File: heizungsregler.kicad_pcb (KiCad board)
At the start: 2 copper layers, 3 parts, among them J101 RPi_GPIO, J105 Conn_01x04_Male, U101 oled_0.96

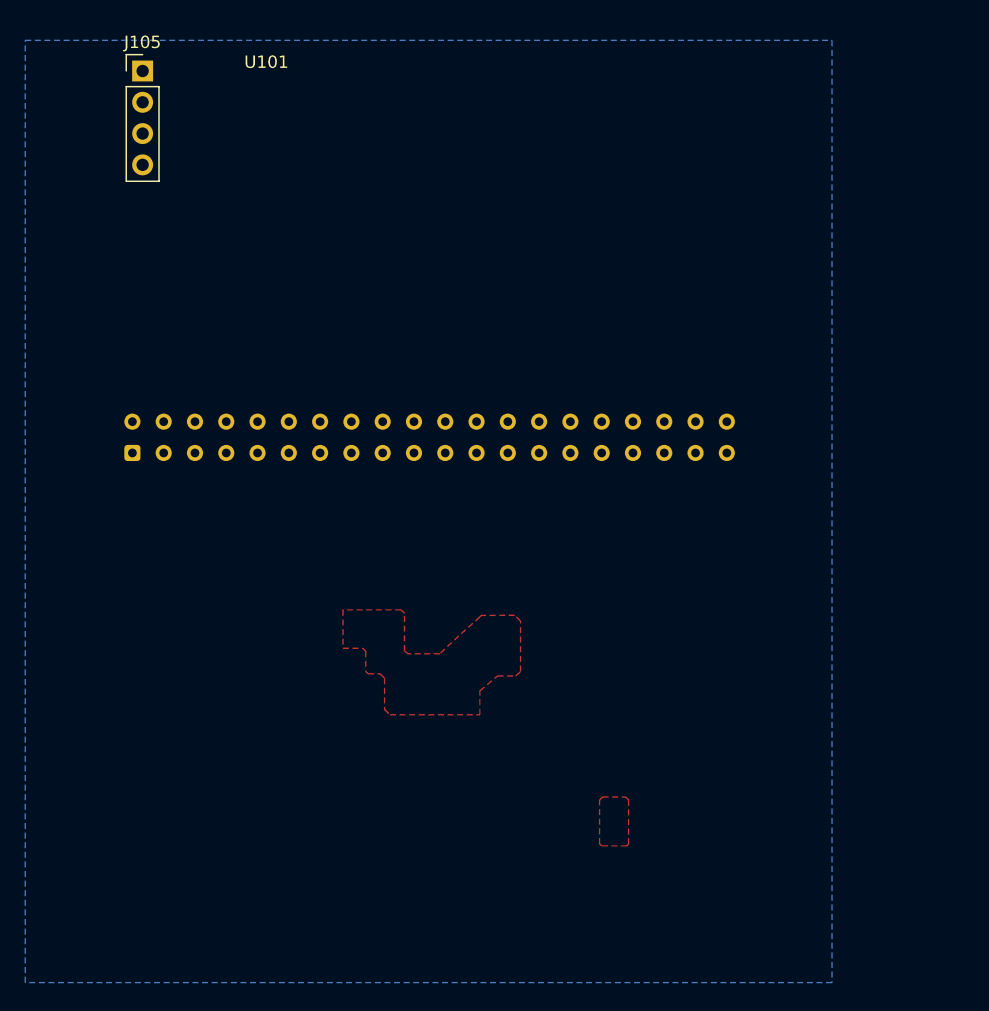
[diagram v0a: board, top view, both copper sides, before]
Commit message: Masseflächen zwischen Leitungen
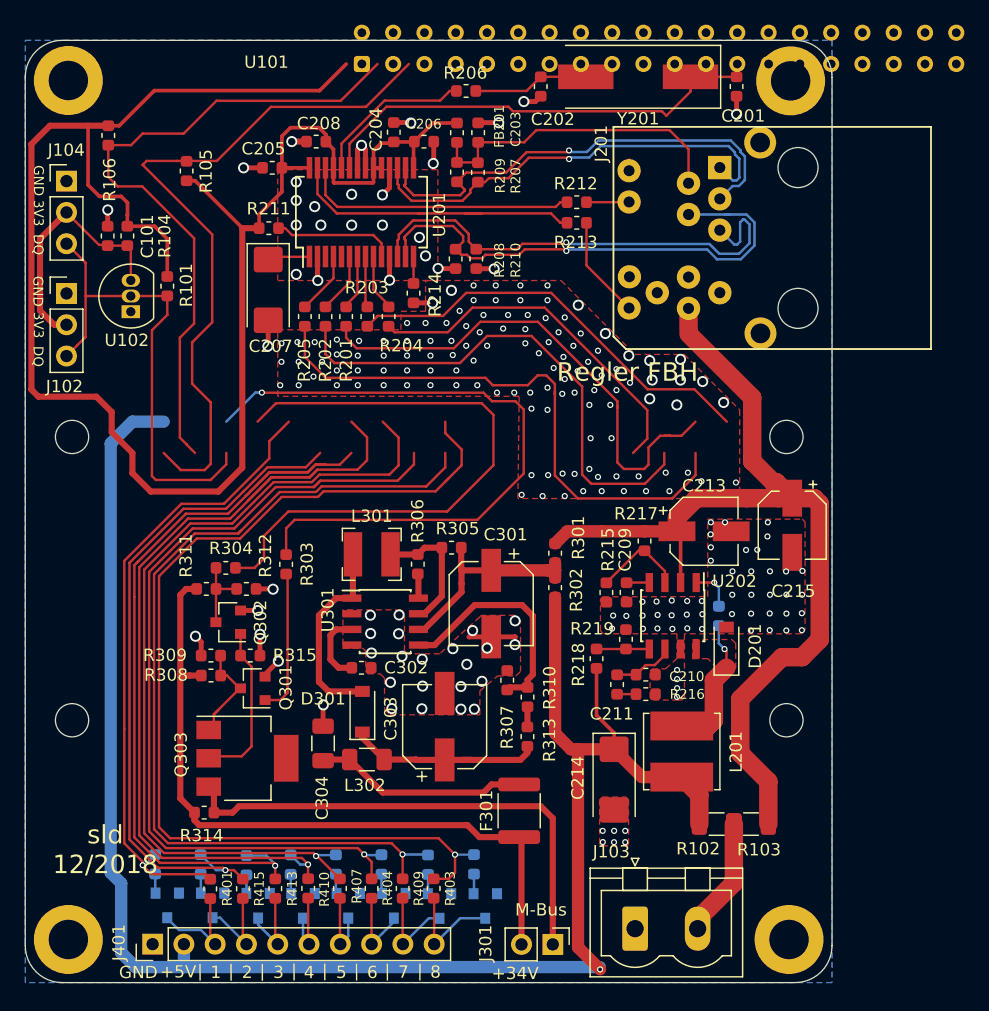
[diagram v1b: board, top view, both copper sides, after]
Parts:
- removed J101: RPi_GPIO, Connector_Samtec_HLE_THT:Samtec_HLE-120-02-xx-DV-TE_2x20_P2.54mm_Horizontal
- removed J105: Conn_01x04_Male, Connector_PinHeader_2.54mm:PinHeader_1x04_P2.54mm_Vertical
- added C101: C, Capacitor_SMD:C_0603_1608Metric, F.Cu at (120.2, 67.4)
- added C201: 22P, Capacitor_SMD:C_0603_1608Metric, F.Cu at (171.2, 55.2)
- added C202: 22P, Capacitor_SMD:C_0603_1608Metric, F.Cu at (155.3, 55.2)
- added C203: 100N, Capacitor_SMD:C_0603_1608Metric, F.Cu at (150.3, 59.0)
- added C204: 100N, Capacitor_SMD:C_0603_1608Metric, F.Cu at (143.4, 59.0)
- added C205: 100N, Capacitor_SMD:C_0603_1608Metric, F.Cu at (133.6, 61.9)
- added C206: 100N, Capacitor_SMD:C_0603_1608Metric, F.Cu at (145.9, 59.7)
- added C207: 10U, Capacitor_Tantalum_SMD:CP_EIA-6032-28_Kemet-C, F.Cu at (133.2, 71.8)
- added C208: 100N, Capacitor_SMD:C_0603_1608Metric, F.Cu at (137.1, 59.7)
- added C209: 8N2, Capacitor_SMD:C_0603_1608Metric, F.Cu at (162.3, 96.3)
- added C210: 82P, Capacitor_SMD:C_0603_1608Metric, F.Cu at (163.9, 103.0)
- added C211: 4N3, Capacitor_SMD:C_0603_1608Metric, F.Cu at (161.6, 103.8)
- added C212: 100N, Capacitor_SMD:C_0603_1608Metric, B.Cu at (169.8, 98.2)
- added C213: 10U, Capacitor_SMD:CP_Elec_5x5.4, F.Cu at (168.6, 91.4)
- added C214: 47U, Capacitor_Tantalum_SMD:CP_EIA-6032-28_Kemet-C, F.Cu at (161.3, 111.5)
- added C215: 10U, Capacitor_SMD:CP_Elec_5x5.4, F.Cu at (175.8, 90.9)
- added C301: 22U, Capacitor_SMD:CP_Elec_6.3x5.7, F.Cu at (151.3, 97.2)
- added C302: 330P, Capacitor_SMD:C_0603_1608Metric, F.Cu at (140.8, 102.4)
- added C303: 47U, Capacitor_SMD:CP_Elec_6.3x7.7, F.Cu at (147.6, 107.2)
- added C304: 1U, Capacitor_SMD:C_1206_3216Metric, F.Cu at (137.7, 108.6)
- added D201: D_Schottky, Diode_SMD:D_SOD-123, F.Cu at (170.4, 100.8)
- added D301: D_Schottky, Diode_SMD:D_SOD-123, F.Cu at (140.9, 106.0)
- added F301: Fuse 2A, Fuse:Fuse_1812_4532Metric, F.Cu at (153.6, 114.0)
- added FB201: Ferrite_Bead, Inductor_SMD:L_0603_1608Metric, F.Cu at (148.6, 59.0)
- added H101: MountingHole, MountingHole:MountingHole_2.7mm_M2.5_DIN965, F.Cu at (117.3, 106.7)
- added H102: MountingHole, MountingHole:MountingHole_2.7mm_M2.5_DIN965, F.Cu at (175.3, 106.7)
- added H103: MountingHole, MountingHole:MountingHole_2.7mm_M2.5_DIN965, F.Cu at (175.3, 83.7)
- added H104: MountingHole, MountingHole:MountingHole_2.7mm_M2.5_DIN965, F.Cu at (117.3, 83.7)
- added H105: MountingHole, MountingHole:MountingHole_3.2mm_M3_DIN965_Pad, F.Cu at (175.6, 54.8)
- added H106: MountingHole, MountingHole:MountingHole_3.2mm_M3_DIN965_Pad, F.Cu at (117.0, 124.5)
- added H107: MountingHole, MountingHole:MountingHole_3.2mm_M3_DIN965_Pad, F.Cu at (175.5, 124.5)
- added H108: MountingHole, MountingHole:MountingHole_3.2mm_M3_DIN965_Pad, F.Cu at (117.0, 54.8)
- added J102: Conn_01x03_Male, Connector_PinHeader_2.54mm:PinHeader_1x03_P2.54mm_Vertical, F.Cu at (116.8, 72.0)
- added J103: Conn_01x02, Connector_Phoenix_MSTB:PhoenixContact_MSTBVA_2,5_2-G-5,08_1x02_P5.08mm_Vertical, F.Cu at (163.0, 123.6)
- added J104: Conn_01x03_Male, Connector_PinHeader_2.54mm:PinHeader_1x03_P2.54mm_Vertical, F.Cu at (116.8, 62.9)
- added J201: SI-52008-F, kicadlibs:RJ45_BEL_STEWART_SI-52008-F, F.Cu at (169.9, 61.8)
- added J301: Conn_01x02_Male, Connector_PinHeader_2.54mm:PinHeader_1x02_P2.54mm_Vertical, F.Cu at (156.3, 124.9)
- added J401: Conn_01x10_Male, Connector_PinHeader_2.54mm:PinHeader_1x10_P2.54mm_Vertical, F.Cu at (123.8, 124.9)
- added L201: 22U, Inductor_SMD:L_Bourns_SRN6045TA, F.Cu at (166.8, 109.2)
- added L301: 150U, Inductor_SMD:L_Bourns-SRN4018, F.Cu at (141.6, 93.2)
- added L302: 1U, Inductor_SMD:L_1206_3216Metric, F.Cu at (141.2, 109.9)
- added Q301: BC847, Package_TO_SOT_SMD:SOT-23, F.Cu at (132.0, 104.1)
- added Q302: BC847, Package_TO_SOT_SMD:SOT-23, F.Cu at (130.0, 98.7)
- added Q303: BCP51, Package_TO_SOT_SMD:SOT-223, F.Cu at (131.5, 109.8)
- added Q401: BC847, Package_TO_SOT_SMD:SOT-23, B.Cu at (125.0, 121.7)
- added Q402: BC847, Package_TO_SOT_SMD:SOT-23, B.Cu at (150.8, 121.8)
- added Q403: BC847, Package_TO_SOT_SMD:SOT-23, B.Cu at (143.4, 121.8)
- added Q404: BC847, Package_TO_SOT_SMD:SOT-23, B.Cu at (139.7, 121.8)
- added Q405: BC847, Package_TO_SOT_SMD:SOT-23, B.Cu at (147.1, 121.8)
- added Q406: BC847, Package_TO_SOT_SMD:SOT-23, B.Cu at (136.1, 121.8)
- added Q407: BC847, Package_TO_SOT_SMD:SOT-23, B.Cu at (132.4, 121.8)
- added Q408: BC847, Package_TO_SOT_SMD:SOT-23, B.Cu at (128.7, 121.7)
- added R101: R, Resistor_SMD:R_0603_1608Metric, F.Cu at (125.0, 71.5)
- added R102: 0R00, Resistor_SMD:R_1206_3216Metric, F.Cu at (169.6, 115.1)
- added R103: 0R00, Resistor_SMD:R_1206_3216Metric, F.Cu at (172.4, 115.1)
- added R104: R, Resistor_SMD:R_0603_1608Metric, F.Cu at (121.8, 67.4)
- added R105: 2K2, Resistor_SMD:R_0603_1608Metric, F.Cu at (126.6, 62.1)
- added R106: 2K2, Resistor_SMD:R_0603_1608Metric, F.Cu at (120.2, 59.2)
- added R201: 0R00, Resistor_SMD:R_0603_1608Metric, F.Cu at (139.6, 73.9)
- added R202: 0R00, Resistor_SMD:R_0603_1608Metric, F.Cu at (137.9, 73.9)
- added R203: 0R00, Resistor_SMD:R_0603_1608Metric, F.Cu at (141.3, 73.9)
- added R204: 0R00, Resistor_SMD:R_0603_1608Metric, F.Cu at (143.0, 73.9)
- added R205: 0R00, Resistor_SMD:R_0603_1608Metric, F.Cu at (136.2, 73.9)
- added R206: 0R00, Resistor_SMD:R_0603_1608Metric, F.Cu at (149.3, 55.6)
- added R207: 49R9, Resistor_SMD:R_0603_1608Metric, F.Cu at (150.2, 62.2)
- added R208: 49R9, Resistor_SMD:R_0603_1608Metric, F.Cu at (148.4, 69.2)
- added R209: 49R9, Resistor_SMD:R_0603_1608Metric, F.Cu at (148.6, 62.2)
- added R210: 49R9, Resistor_SMD:R_0603_1608Metric, F.Cu at (150.1, 69.2)
- added R211: 0R00, Resistor_SMD:R_0603_1608Metric, F.Cu at (133.3, 66.8)
- added R212: 220R, Resistor_SMD:R_0603_1608Metric, F.Cu at (158.3, 64.6)
- added R213: 220R, Resistor_SMD:R_0603_1608Metric, F.Cu at (158.3, 66.3)
- added R214: 2K32, Resistor_SMD:R_0603_1608Metric, F.Cu at (145.0, 72.0)
- added R215: 19K6, Resistor_SMD:R_0603_1608Metric, F.Cu at (160.7, 96.3)
- added R216: 18K7, Resistor_SMD:R_0603_1608Metric, F.Cu at (163.9, 104.6)
- added R217: 169K, Resistor_SMD:R_0603_1608Metric, F.Cu at (163.8, 92.2)
- added R218: 10K2, Resistor_SMD:R_0603_1608Metric, F.Cu at (159.9, 101.7)
- added R219: 1K96, Resistor_SMD:R_0603_1608Metric, F.Cu at (162.3, 100.1)
- added R301: 0R00, Resistor_SMD:R_0603_1608Metric, F.Cu at (156.5, 93.1)
- added R302: 0R00, Resistor_SMD:R_0603_1608Metric, F.Cu at (156.5, 95.9)
- added R303: 1K, Resistor_SMD:R_0603_1608Metric, F.Cu at (134.7, 94.0)
- added R304: 1K, Resistor_SMD:R_0603_1608Metric, F.Cu at (129.8, 94.3)
- added R305: 0R47, Resistor_SMD:R_0603_1608Metric, F.Cu at (148.1, 92.7)
- added R306: 180, Resistor_SMD:R_0603_1608Metric, F.Cu at (145.4, 94.0)
- added R307: 4k7, Resistor_SMD:R_0603_1608Metric, F.Cu at (152.6, 103.5)
- added R308: 39K, Resistor_SMD:R_0603_1608Metric, F.Cu at (128.6, 103.1)
- added R309: 22K, Resistor_SMD:R_0603_1608Metric, F.Cu at (128.6, 101.5)
- added R310: 100K, Resistor_SMD:R_0603_1608Metric, F.Cu at (154.3, 104.8)
- added R311: 33K, Resistor_SMD:R_0603_1608Metric, F.Cu at (128.2, 96.0)
- added R312: 3K3, Resistor_SMD:R_0603_1608Metric, F.Cu at (131.5, 96.0)
- added R313: 22K, Resistor_SMD:R_0603_1608Metric, F.Cu at (154.3, 108.0)
- added R314: 220K, Resistor_SMD:R_0603_1608Metric, F.Cu at (128.0, 114.2)
- added R315: 82R, Resistor_SMD:R_0603_1608Metric, F.Cu at (131.8, 101.5)
- added R401: R, Resistor_SMD:R_0603_1608Metric, F.Cu at (128.5, 120.4)
- added R402: R, Resistor_SMD:R_0603_1608Metric, B.Cu at (124.0, 118.4)
- added R403: R, Resistor_SMD:R_0603_1608Metric, F.Cu at (146.7, 120.4)
- added R404: R, Resistor_SMD:R_0603_1608Metric, F.Cu at (141.6, 120.4)
- added R405: R, Resistor_SMD:R_0603_1608Metric, B.Cu at (149.9, 118.4)
- added R406: R, Resistor_SMD:R_0603_1608Metric, B.Cu at (142.4, 118.4)
- added R407: R, Resistor_SMD:R_0603_1608Metric, F.Cu at (139.1, 120.4)
- added R408: R, Resistor_SMD:R_0603_1608Metric, B.Cu at (138.7, 118.4)
- added R409: R, Resistor_SMD:R_0603_1608Metric, F.Cu at (144.1, 120.4)
- added R410: R, Resistor_SMD:R_0603_1608Metric, F.Cu at (136.5, 120.3)
- added R411: R, Resistor_SMD:R_0603_1608Metric, B.Cu at (146.2, 118.4)
- added R412: R, Resistor_SMD:R_0603_1608Metric, B.Cu at (135.1, 118.4)
- added R413: R, Resistor_SMD:R_0603_1608Metric, F.Cu at (133.8, 120.4)
- added R414: R, Resistor_SMD:R_0603_1608Metric, B.Cu at (131.5, 118.5)
- added R415: R, Resistor_SMD:R_0603_1608Metric, F.Cu at (131.2, 120.4)
- added R416: R, Resistor_SMD:R_0603_1608Metric, B.Cu at (127.7, 118.4)
- added U102: DS18B20, Package_TO_SOT_THT:TO-92_Inline, F.Cu at (122.1, 73.5)
- added U201: ENC28J60x-SS, Package_SO:SSOP-28_5.3x10.2mm_P0.65mm, F.Cu at (140.8, 65.5)
- added U202: TPS54231, Package_SO:SOIC-8_3.9x4.9mm_P1.27mm, F.Cu at (166.1, 98.2)
- added U301: MC34063AD, Package_SO:SOIC-8_3.9x4.9mm_P1.27mm, F.Cu at (142.7, 98.7)
- added Y201: Crystal, Crystal:Crystal_SMD_HC49-SD, F.Cu at (163.3, 54.5)
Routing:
- net +3V3: track 0.00 -> 152.0 mm
- net +5V: track 0.00 -> 141.0 mm, vias 0 -> 1
- net /REL8: track 0.00 -> 83.1 mm, vias 0 -> 1
- net +24V: track 0.00 -> 77.8 mm
- net /REL7: track 0.00 -> 74.6 mm, vias 0 -> 1
- net /REL4: track 0.00 -> 71.8 mm, vias 0 -> 1
- net /REL6: track 0.00 -> 69.6 mm, vias 0 -> 1
- net /REL5: track 0.00 -> 68.8 mm, vias 0 -> 1
- net /REL3: track 0.00 -> 67.4 mm, vias 0 -> 1
- net +36V: track 0.00 -> 57.7 mm
- net /SDA: track 0.00 -> 57.5 mm
- net /REL2: track 0.00 -> 54.7 mm, vias 0 -> 1
- net /SCL: track 0.00 -> 54.6 mm
- net /TXD: track 0.00 -> 54.2 mm, vias 0 -> 1
- net /REL1: track 0.00 -> 51.6 mm, vias 0 -> 1
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- added copper zone on F.Cu, net Net-(C212-Pad1)
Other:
- board outline added: 65.5 x 76.5 mm
- board text added: "+34V"
- board text added: "+5V"
- board text added: "1"
- board text added: "2"
- board text added: "3"
- board text added: "3V3"
- board text added: "4"
- board text added: "5"
- board text added: "6"
- board text added: "7"
- board text added: "8"
- board text added: "DQ"
- board text added: "GND"
- board text added: "M-Bus"
- board text added: "Regler FBH"
- board text added: "sld 12/2018"
- board text added: "|"

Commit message: Änderungen nach Review, Layout fertig
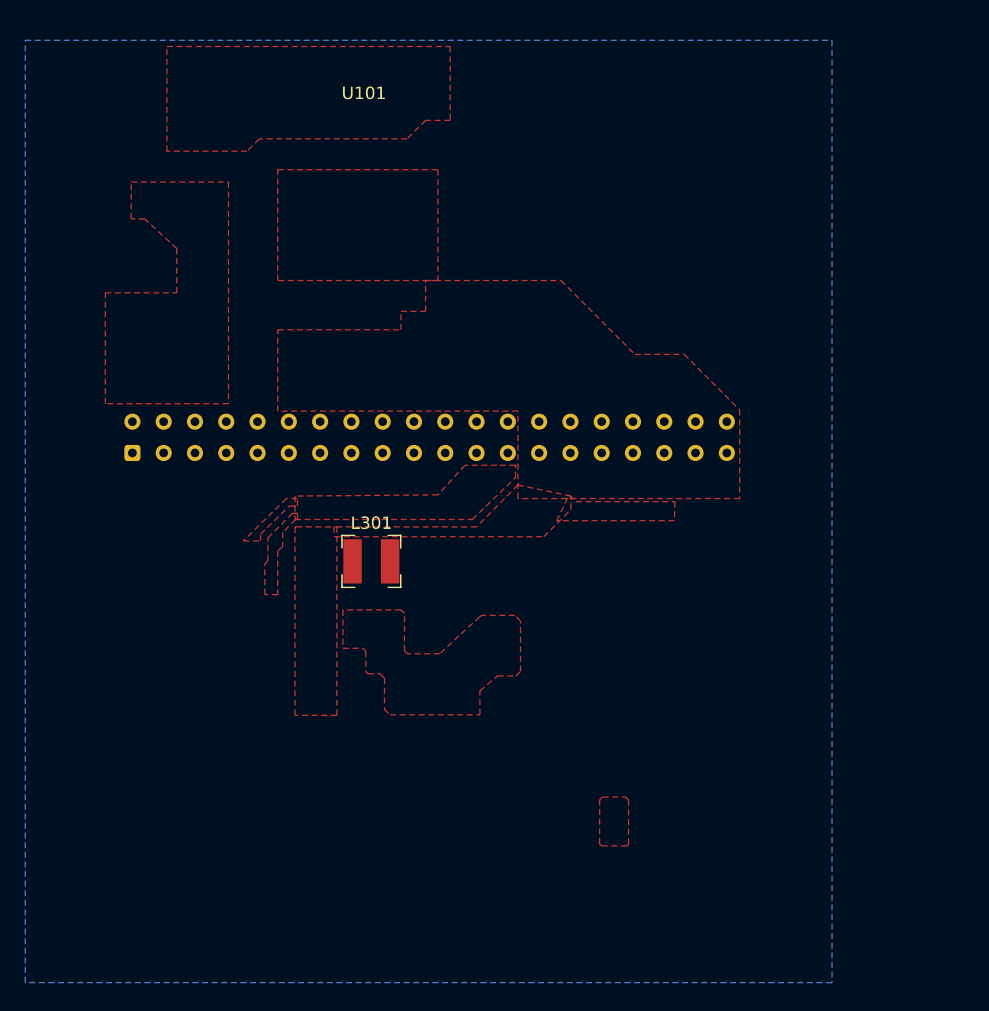
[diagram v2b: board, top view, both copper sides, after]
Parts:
- removed C101: C, Capacitor_SMD:C_0603_1608Metric
- removed C201, C202: 22P, Capacitor_SMD:C_0603_1608Metric
- removed C203, C204, C205, C206, C208, C212: 100N, Capacitor_SMD:C_0603_1608Metric
- removed C207: 10U, Capacitor_Tantalum_SMD:CP_EIA-6032-28_Kemet-C
- removed C209: 8N2, Capacitor_SMD:C_0603_1608Metric
- removed C210: 82P, Capacitor_SMD:C_0603_1608Metric
- removed C211: 4N3, Capacitor_SMD:C_0603_1608Metric
- removed C213, C215: 10U, Capacitor_SMD:CP_Elec_5x5.4
- removed C214: 47U, Capacitor_Tantalum_SMD:CP_EIA-6032-28_Kemet-C
- removed C301: 22U, Capacitor_SMD:CP_Elec_6.3x5.7
- removed C302: 330P, Capacitor_SMD:C_0603_1608Metric
- removed C303: 47U, Capacitor_SMD:CP_Elec_6.3x7.7
- removed C304: 1U, Capacitor_SMD:C_1206_3216Metric
- removed D201, D301: D_Schottky, Diode_SMD:D_SOD-123
- removed F301: Fuse 2A, Fuse:Fuse_1812_4532Metric
- removed FB201: Ferrite_Bead, Inductor_SMD:L_0603_1608Metric
- removed H101, H102, H103, H104: MountingHole, MountingHole:MountingHole_2.7mm_M2.5_DIN965
- removed H105, H106, H107, H108: MountingHole, MountingHole:MountingHole_3.2mm_M3_DIN965_Pad
- removed J102, J104: Conn_01x03_Male, Connector_PinHeader_2.54mm:PinHeader_1x03_P2.54mm_Vertical
- removed J103: Conn_01x02, Connector_Phoenix_MSTB:PhoenixContact_MSTBVA_2,5_2-G-5,08_1x02_P5.08mm_Vertical
- removed J201: SI-52008-F, kicadlibs:RJ45_BEL_STEWART_SI-52008-F
- removed J301: Conn_01x02_Male, Connector_PinHeader_2.54mm:PinHeader_1x02_P2.54mm_Vertical
- removed J401: Conn_01x10_Male, Connector_PinHeader_2.54mm:PinHeader_1x10_P2.54mm_Vertical
- removed L201: 22U, Inductor_SMD:L_Bourns_SRN6045TA
- removed L302: 1U, Inductor_SMD:L_1206_3216Metric
- removed Q301, Q302, Q401, Q402, Q403, Q404, Q405, Q406, Q407, Q408: BC847, Package_TO_SOT_SMD:SOT-23
- removed Q303: BCP51, Package_TO_SOT_SMD:SOT-223
- removed R101, R104, R401, R402, R403, R404, R405, R406, R407, R408, R409, R410, R411, R412, R413, R414, R415, R416: R, Resistor_SMD:R_0603_1608Metric
- removed R102, R103: 0R00, Resistor_SMD:R_1206_3216Metric
- removed R105, R106: 2K2, Resistor_SMD:R_0603_1608Metric
- removed R201, R202, R203, R204, R205, R206, R211, R301, R302: 0R00, Resistor_SMD:R_0603_1608Metric
- removed R207, R208, R209, R210: 49R9, Resistor_SMD:R_0603_1608Metric
- removed R212, R213: 220R, Resistor_SMD:R_0603_1608Metric
- removed R214: 2K32, Resistor_SMD:R_0603_1608Metric
- removed R215: 19K6, Resistor_SMD:R_0603_1608Metric
- removed R216: 18K7, Resistor_SMD:R_0603_1608Metric
- removed R217: 169K, Resistor_SMD:R_0603_1608Metric
- removed R218: 10K2, Resistor_SMD:R_0603_1608Metric
- removed R219: 1K96, Resistor_SMD:R_0603_1608Metric
- removed R303, R304: 1K, Resistor_SMD:R_0603_1608Metric
- removed R305: 0R47, Resistor_SMD:R_0603_1608Metric
- removed R306: 180, Resistor_SMD:R_0603_1608Metric
- removed R307: 4k7, Resistor_SMD:R_0603_1608Metric
- removed R308: 39K, Resistor_SMD:R_0603_1608Metric
- removed R309, R313: 22K, Resistor_SMD:R_0603_1608Metric
- removed R310: 100K, Resistor_SMD:R_0603_1608Metric
- removed R311: 33K, Resistor_SMD:R_0603_1608Metric
- removed R312: 3K3, Resistor_SMD:R_0603_1608Metric
- removed R314: 220K, Resistor_SMD:R_0603_1608Metric
- removed R315: 82R, Resistor_SMD:R_0603_1608Metric
- removed U102: DS18B20, Package_TO_SOT_THT:TO-92_Inline
- removed U201: ENC28J60x-SS, Package_SO:SSOP-28_5.3x10.2mm_P0.65mm
- removed U202: TPS54231, Package_SO:SOIC-8_3.9x4.9mm_P1.27mm
- removed U301: MC34063AD, Package_SO:SOIC-8_3.9x4.9mm_P1.27mm
- removed Y201: Crystal, Crystal:Crystal_SMD_HC49-SD
- added J101: RPi_GPIO, Connector_Samtec_HLE_THT:Samtec_HLE-120-02-xx-DV-TE_2x20_P2.54mm_Horizontal, B.Cu at (122.2, 85.0)
- L301: value 150U -> 270U
- moved L301 0.57 mm to (141.6, 93.8)
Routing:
- net +3V3: track 152.0 -> 0.00 mm
- net +5V: track 141.0 -> 0.00 mm, vias 1 -> 0
- net /REL8: track 83.1 -> 0.00 mm, vias 1 -> 0
- net +24V: track 77.8 -> 0.00 mm
- net /REL7: track 74.6 -> 0.00 mm, vias 1 -> 0
- net /REL4: track 71.8 -> 0.00 mm, vias 1 -> 0
- net /REL6: track 69.6 -> 0.00 mm, vias 1 -> 0
- net /REL5: track 68.8 -> 0.00 mm, vias 1 -> 0
- net /REL3: track 67.4 -> 0.00 mm, vias 1 -> 0
- net +36V: track 57.7 -> 0.00 mm
- net /SDA: track 57.5 -> 0.00 mm
- net /REL2: track 54.7 -> 0.00 mm, vias 1 -> 0
- net /SCL: track 54.6 -> 0.00 mm
- net /TXD: track 54.2 -> 0.00 mm, vias 1 -> 0
- net /REL1: track 51.6 -> 0.00 mm, vias 1 -> 0
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- removed copper zone on F.Cu, net Net-(C212-Pad1)
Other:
- board outline removed
- board text removed: "+34V"
- board text removed: "+5V"
- board text removed: "1"
- board text removed: "2"
- board text removed: "3"
- board text removed: "3V3"
- board text removed: "4"
- board text removed: "5"
- board text removed: "6"
- board text removed: "7"
- board text removed: "8"
- board text removed: "DQ"
- board text removed: "GND"
- board text removed: "M-Bus"
- board text removed: "Regler FBH"
- board text removed: "sld 12/2018"
- board text removed: "|"

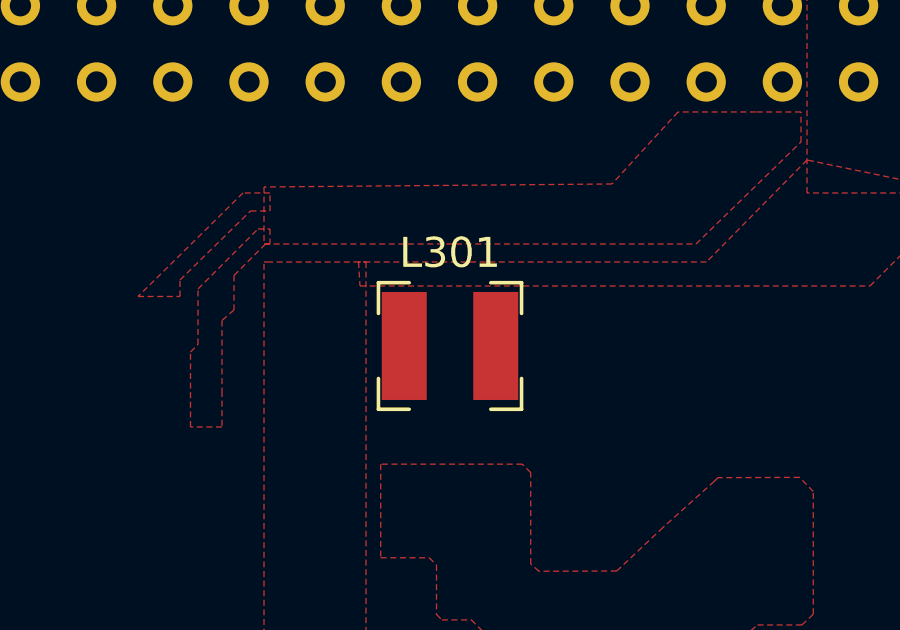
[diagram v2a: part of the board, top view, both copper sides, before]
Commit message: Footprint katualisiert, klitzekleine Aenderungen
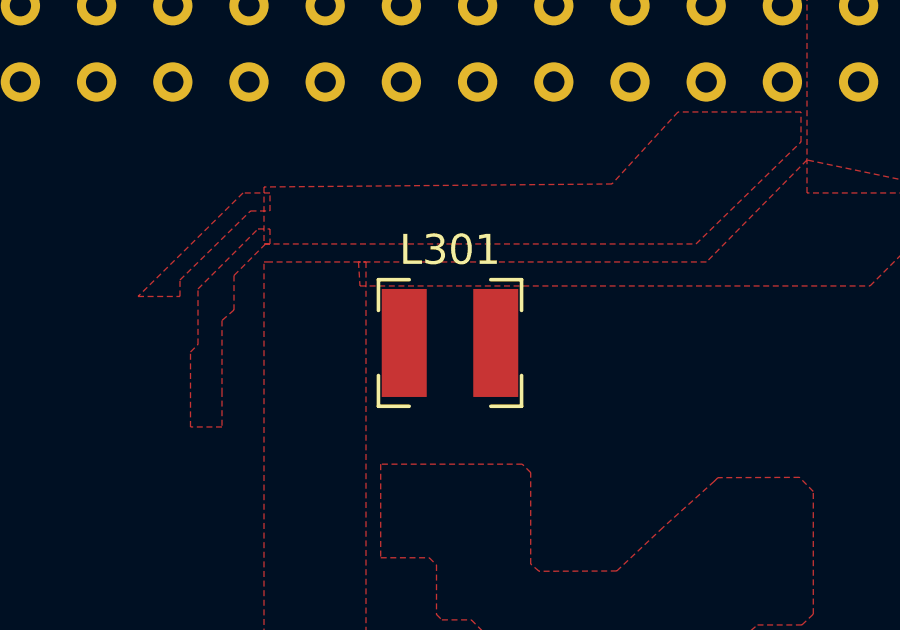
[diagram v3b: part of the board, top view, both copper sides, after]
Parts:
- moved L301 0.10 mm to (141.6, 93.7)
